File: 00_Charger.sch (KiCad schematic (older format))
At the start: 42 parts, among them J401 TB001-500-02BE CUI_Devices, Q401 NTK3043N, Q402 FDD4685-F085, U401 MAX1873TEEE, U402 PC827

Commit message: fertig zum routen
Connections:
- net GNDPWR is gone; now on net GND: J401.1 (Pin_1)
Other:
- note removed: "GND über Shunt verbinden"
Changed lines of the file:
@@
 Text Notes 3500 1600 0    50   ~ 0
 Spannung 20V in Ladekabel
-$Comp
-L power:GNDPWR #PWR0401
-U 1 1 5E8B9696
-P 2250 2600
-F 0 "#PWR0401" H 2250 2400 50  0001 C CNN
-F 1 "GNDPWR" H 2254 2446 50  0000 C CNN
-F 2 "" H 2250 2550 50  0001 C CNN
-F 3 "" H 2250 2550 50  0001 C CNN
-	1    2250 2600
-	1    0    0    -1
-$EndComp
-Wire Wire Line
-	2250 2600 2250 2300
-Text Notes 1850 1900 0    50   ~ 0
-GND über Shunt verbinden
 Text Label 3300 2200 0    50   ~ 0
 DC_20V_POWER_SUPPLY
@@
 Wire Wire Line
 	9000 3900 9000 3750
+$Comp
+L power:GND #PWR0191
+U 1 1 5E980EB1
+P 2250 3100
+F 0 "#PWR0191" H 2250 2850 50  0001 C CNN
+F 1 "GND" H 2255 2927 50  0000 C CNN
+F 2 "" H 2250 3100 50  0001 C CNN
+F 3 "" H 2250 3100 50  0001 C CNN
+	1    2250 3100
+	1    0    0    -1
+$EndComp
+Wire Wire Line
+	2250 2300 2250 3100
 $EndSCHEMATC

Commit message: Fertig zum letzten Check vor Bestellung
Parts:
- C411: footprint Capacitor_SMD:CP_Elec_5x5.4 -> Capacitor_THT:CP_Radial_D6.3mm_P2.50mm
- C412: footprint Capacitor_SMD:CP_Elec_5x5.4 -> Capacitor_THT:CP_Radial_D5.0mm_P2.50mm
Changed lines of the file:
@@
 F 0 "C411" H 8741 4196 50  0000 L CNN
 F 1 "68u" H 8741 4105 50  0000 L CNN
-F 2 "Capacitor_SMD:CP_Elec_5x5.4" H 8650 4150 50  0001 C CNN
+F 2 "Capacitor_THT:CP_Radial_D6.3mm_P2.50mm" H 8650 4150 50  0001 C CNN
 F 3 "~" H 8650 4150 50  0001 C CNN
 	1    8650 4150
@@
 F 0 "C412" H 9391 3546 50  0000 L CNN
 F 1 "47u" H 9391 3455 50  0000 L CNN
-F 2 "Capacitor_SMD:CP_Elec_5x5.4" H 9300 3500 50  0001 C CNN
+F 2 "Capacitor_THT:CP_Radial_D5.0mm_P2.50mm" H 9300 3500 50  0001 C CNN
 F 3 "~" H 9300 3500 50  0001 C CNN
 	1    9300 3500

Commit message: Board abgeschickt
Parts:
- C401: value 1u -> 1uF
- C402, C403, C405, C406: value 220n -> 220nF
- C404: value 2.2u -> 2.2uF
- C407, C408: value 47n -> 47nF
- C409: value 1n -> 1nF
- C410: value 0.1u -> 100nF
- C411: value 68u -> 68uF
- C412: value 47u -> 68uF
- HS401, HS402, HS403: value Heatsink_Pad -> 573300D00000G
- R417: value 100K -> 1M
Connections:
- net CHARGER_DISABLE: now also R417.1
- net at Q401.1 (G), R415.2: no longer R417.1
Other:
- moved on the sheet: R415, R417
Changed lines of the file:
@@
 P 7350 4450
 F 0 "C408" V 7400 4100 50  0000 C CNN
-F 1 "47n" V 7400 4300 50  0000 C CNN
+F 1 "47nF" V 7400 4300 50  0000 C CNN
 F 2 "Capacitor_SMD:C_0603_1608Metric_Pad1.05x0.95mm_HandSolder" H 7350 4450 50  0001 C CNN
 F 3 "~" H 7350 4450 50  0001 C CNN
@@
 P 5050 4050
 F 0 "C401" H 4958 4004 50  0000 R CNN
-F 1 "1u" H 4958 4095 50  0000 R CNN
+F 1 "1uF" H 4958 4095 50  0000 R CNN
 F 2 "Capacitor_SMD:C_0603_1608Metric_Pad1.05x0.95mm_HandSolder" H 5050 4050 50  0001 C CNN
 F 3 "~" H 5050 4050 50  0001 C CNN
@@
 P 7350 4950
 F 0 "C409" V 7400 4650 50  0000 C CNN
-F 1 "1n" V 7400 4850 50  0000 C CNN
+F 1 "1nF" V 7400 4850 50  0000 C CNN
 F 2 "Capacitor_SMD:C_0603_1608Metric_Pad1.05x0.95mm_HandSolder" H 7350 4950 50  0001 C CNN
 F 3 "~" H 7350 4950 50  0001 C CNN
@@
 P 5450 3100
 F 0 "C402" V 5221 3100 50  0000 C CNN
-F 1 "220n" V 5312 3100 50  0000 C CNN
+F 1 "220nF" V 5312 3100 50  0000 C CNN
 F 2 "Capacitor_SMD:C_0603_1608Metric_Pad1.05x0.95mm_HandSolder" H 5450 3100 50  0001 C CNN
 F 3 "~" H 5450 3100 50  0001 C CNN
@@
 P 7350 4300
 F 0 "C407" V 7400 3950 50  0000 C CNN
-F 1 "47n" V 7400 4150 50  0000 C CNN
+F 1 "47nF" V 7400 4150 50  0000 C CNN
 F 2 "Capacitor_SMD:C_0603_1608Metric_Pad1.05x0.95mm_HandSolder" H 7350 4300 50  0001 C CNN
 F 3 "~" H 7350 4300 50  0001 C CNN
@@
 U 1 1 5E7803AB
 P 7850 4600
-F 0 "C410" V 7950 4350 50  0000 C CNN
-F 1 "0.1u" V 7900 4500 50  0000 C CNN
+F 0 "C410" V 7750 4450 50  0000 C CNN
+F 1 "100nF" V 7650 4450 50  0000 C CNN
 F 2 "Capacitor_SMD:C_0603_1608Metric_Pad1.05x0.95mm_HandSolder" H 7850 4600 50  0001 C CNN
 F 3 "~" H 7850 4600 50  0001 C CNN
@@
 P 5700 2900
 F 0 "C403" V 5471 2900 50  0000 C CNN
-F 1 "220n" V 5562 2900 50  0000 C CNN
+F 1 "220nF" V 5562 2900 50  0000 C CNN
 F 2 "Capacitor_SMD:C_0603_1608Metric_Pad1.05x0.95mm_HandSolder" H 5700 2900 50  0001 C CNN
 F 3 "~" H 5700 2900 50  0001 C CNN
@@
 P 6600 2450
 F 0 "C404" V 6371 2450 50  0000 C CNN
-F 1 "2.2u" V 6462 2450 50  0000 C CNN
+F 1 "2.2uF" V 6462 2450 50  0000 C CNN
 F 2 "Capacitor_SMD:C_0603_1608Metric_Pad1.05x0.95mm_HandSolder" H 6600 2450 50  0001 C CNN
 F 3 "~" H 6600 2450 50  0001 C CNN
@@
 P 7300 3000
 F 0 "C405" H 7208 2954 50  0000 R CNN
-F 1 "220n" H 7208 3045 50  0000 R CNN
+F 1 "220nF" H 7208 3045 50  0000 R CNN
 F 2 "Capacitor_SMD:C_0603_1608Metric_Pad1.05x0.95mm_HandSolder" H 7300 3000 50  0001 C CNN
 F 3 "~" H 7300 3000 50  0001 C CNN
@@
 P 7300 3450
 F 0 "C406" H 7208 3404 50  0000 R CNN
-F 1 "220n" H 7208 3495 50  0000 R CNN
+F 1 "220nF" H 7208 3495 50  0000 R CNN
 F 2 "Capacitor_SMD:C_0603_1608Metric_Pad1.05x0.95mm_HandSolder" H 7300 3450 50  0001 C CNN
 F 3 "~" H 7300 3450 50  0001 C CNN
@@
 P 8650 4150
 F 0 "C411" H 8741 4196 50  0000 L CNN
-F 1 "68u" H 8741 4105 50  0000 L CNN
+F 1 "68uF" H 8741 4105 50  0000 L CNN
 F 2 "Capacitor_THT:CP_Radial_D6.3mm_P2.50mm" H 8650 4150 50  0001 C CNN
 F 3 "~" H 8650 4150 50  0001 C CNN
@@
 Text GLabel 3600 3950 0    50   Input ~ 0
 CHARGER_DISABLE
-Wire Wire Line
-	3950 3950 4100 3950
 Text Notes 8900 2450 0    50   ~ 0
 R_CSB - Charge Current Limit\n68m: Icharge = 0.2V/R_CSB = 3A\nfür 2 Zellen Parallel = 0.5Charging Rate\n
@@
 P 9300 3500
 F 0 "C412" H 9391 3546 50  0000 L CNN
-F 1 "47u" H 9391 3455 50  0000 L CNN
+F 1 "68uF" H 9391 3455 50  0000 L CNN
 F 2 "Capacitor_THT:CP_Radial_D5.0mm_P2.50mm" H 9300 3500 50  0001 C CNN
 F 3 "~" H 9300 3500 50  0001 C CNN
@@
 L Device:R_Small R415
 U 1 1 5ECEF6C1
-P 3850 3950
-F 0 "R415" V 3750 4000 50  0000 R CNN
-F 1 "10k" V 3650 4000 50  0000 R CNN
-F 2 "Resistor_SMD:R_0603_1608Metric_Pad1.05x0.95mm_HandSolder" H 3850 3950 50  0001 C CNN
-F 3 "~" H 3850 3950 50  0001 C CNN
-	1    3850 3950
+P 4000 3950
+F 0 "R415" V 3900 4000 50  0000 R CNN
+F 1 "10k" V 3800 4000 50  0000 R CNN
+F 2 "Resistor_SMD:R_0603_1608Metric_Pad1.05x0.95mm_HandSolder" H 4000 3950 50  0001 C CNN
+F 3 "~" H 4000 3950 50  0001 C CNN
+	1    4000 3950
 	0    -1   -1   0
 $EndComp
 Wire Wire Line
-	3750 3950 3600 3950
+	3900 3950 3800 3950
 $Comp
 L Device:R_Small R417
 U 1 1 5EE5F4E2
-P 4100 4350
-F 0 "R417" H 4159 4396 50  0000 L CNN
-F 1 "100K" H 4159 4305 50  0000 L CNN
-F 2 "Resistor_SMD:R_0603_1608Metric_Pad1.05x0.95mm_HandSolder" H 4100 4350 50  0001 C CNN
-F 3 "~" H 4100 4350 50  0001 C CNN
-	1    4100 4350
-	1    0    0    -1
-$EndComp
-Wire Wire Line
-	4100 4250 4100 3950
-Connection ~ 4100 3950
-Wire Wire Line
-	4100 3950 4200 3950
+P 3800 4350
+F 0 "R417" H 3859 4396 50  0000 L CNN
+F 1 "1M" H 3859 4305 50  0000 L CNN
+F 2 "Resistor_SMD:R_0603_1608Metric_Pad1.05x0.95mm_HandSolder" H 3800 4350 50  0001 C CNN
+F 3 "~" H 3800 4350 50  0001 C CNN
+	1    3800 4350
+	1    0    0    -1
+$EndComp
 $Comp
 L power:GND #PWR0407
 U 1 1 5EE6150A
-P 4100 5200
-F 0 "#PWR0407" H 4100 4950 50  0001 C CNN
-F 1 "GND" H 4105 5027 50  0000 C CNN
-F 2 "" H 4100 5200 50  0001 C CNN
-F 3 "" H 4100 5200 50  0001 C CNN
-	1    4100 5200
-	1    0    0    -1
-$EndComp
-Wire Wire Line
-	4100 5200 4100 4450
+P 3800 5200
+F 0 "#PWR0407" H 3800 4950 50  0001 C CNN
+F 1 "GND" H 3805 5027 50  0000 C CNN
+F 2 "" H 3800 5200 50  0001 C CNN
+F 3 "" H 3800 5200 50  0001 C CNN
+	1    3800 5200
+	1    0    0    -1
+$EndComp
+Wire Wire Line
+	3800 5200 3800 4450
 Connection ~ 5550 2200
 $Comp
@@
 P 4750 1450
 F 0 "HS401" H 4891 1491 50  0000 L CNN
-F 1 "Heatsink_Pad" H 4891 1400 50  0000 L CNN
+F 1 "573300D00000G" H 4891 1400 50  0000 L CNN
 F 2 "Heatsink:Heatsink_AAVID_573300D00010G_TO-263" H 4762 1400 50  0001 C CNN
 F 3 "~" H 4762 1400 50  0001 C CNN
@@
 P 8450 3400
 F 0 "HS403" H 8500 4000 50  0000 L CNN
-F 1 "Heatsink_Pad" H 8500 3900 50  0000 L CNN
+F 1 "573300D00000G" H 8500 3900 50  0000 L CNN
 F 2 "Heatsink:Heatsink_AAVID_573300D00010G_TO-263" H 8462 3350 50  0001 C CNN
 F 3 "~" H 8462 3350 50  0001 C CNN
@@
 P 8150 3400
 F 0 "HS402" H 8150 4000 50  0000 L CNN
-F 1 "Heatsink_Pad" H 7950 3900 50  0000 L CNN
+F 1 "573300D00000G" H 7950 3900 50  0000 L CNN
 F 2 "Heatsink:Heatsink_AAVID_573300D00010G_TO-263" H 8162 3350 50  0001 C CNN
 F 3 "~" H 8162 3350 50  0001 C CNN
@@
 Wire Wire Line
 	2250 2300 2250 3100
+Wire Wire Line
+	4100 3950 4200 3950
+Wire Wire Line
+	3800 4250 3800 3950
+Connection ~ 3800 3950
+Wire Wire Line
+	3800 3950 3600 3950
 $EndSCHEMATC

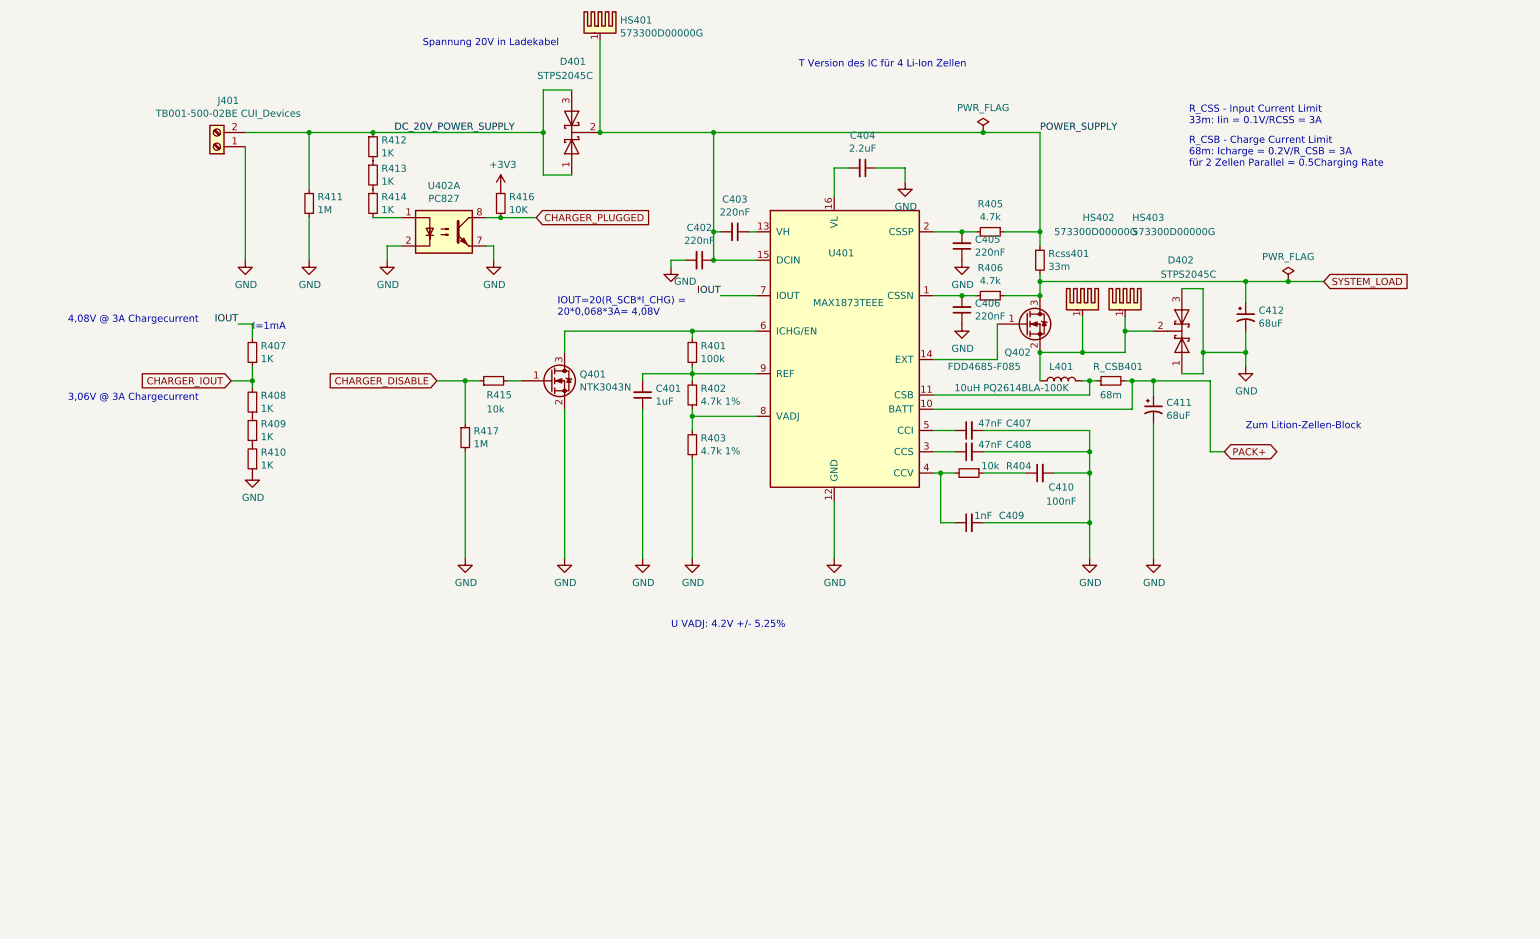
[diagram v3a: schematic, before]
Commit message: mute and stdby tda7498 geändert, tda7418 durch tda7719 ersetzt, xs3868 durch bk8000l ersetzt, 3v3 stepdown statt LDO. BMS gelöscht.  TODO: Möglichkeit stepup und stepdown als modul aufzusetzen
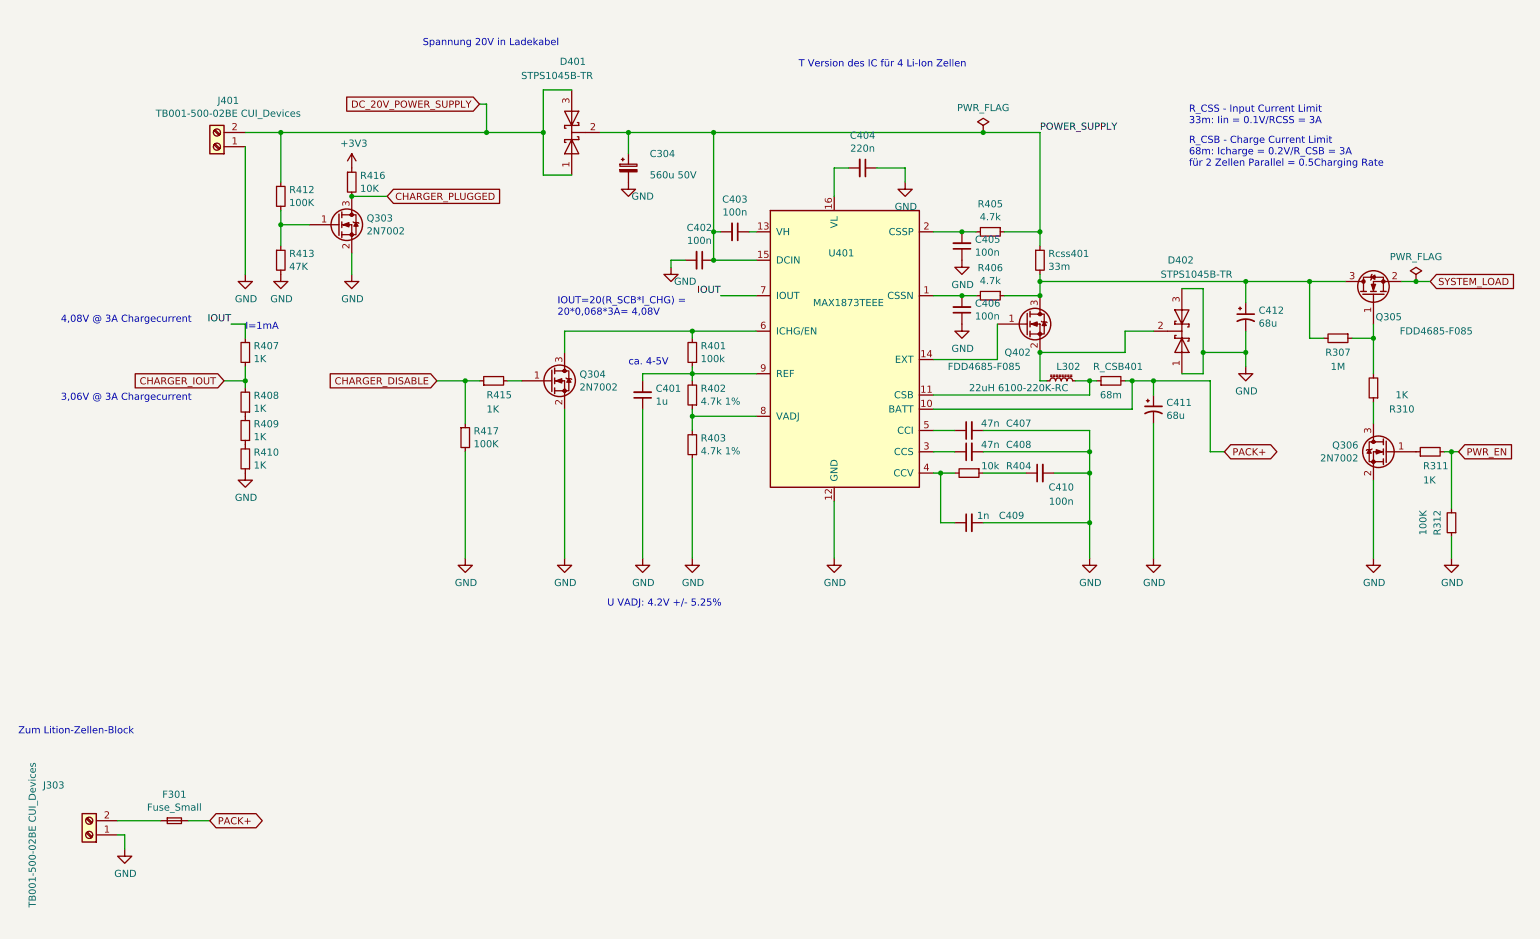
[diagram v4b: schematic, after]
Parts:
- removed HS401, HS402, HS403: 573300D00000G, Heatsink:Heatsink_AAVID_573300D00010G_TO-263, symbol Mechanical:Heatsink_Pad
- removed L401: 10uH PQ2614BLA-100K, Inductor_SMD:PQ2617BHA-330K, symbol Device:L
- removed Q401: NTK3043N, Package_TO_SOT_SMD:SOT-723, symbol Device:Q_NMOS_GSD
- removed R411: 1M, Resistor_SMD:R_0603_1608Metric_Pad1.05x0.95mm_HandSolder, symbol Device:R_Small
- removed R414: 1K, Resistor_SMD:R_0603_1608Metric_Pad1.05x0.95mm_HandSolder, symbol Device:R_Small
- removed U402: PC827, Package_DIP:DIP-8_W7.62mm_SMDSocket_SmallPads, symbol Isolator:PC827
- added C304: 560u 50V, Capacitor_THT:CP_Radial_D12.5mm_P5.00mm, symbol Device:CP_Small
- added F301: Fuse_Small, Fuse:Fuseholder_Cylinder-5x20mm_Schurter_0031-8002_Horizontal_Open, symbol Device:Fuse_Small
- added J303: TB001-500-02BE CUI_Devices, TerminalBlock_RND:TerminalBlock_RND_205-00045_1x02_P5.00mm_Horizontal, symbol Connector:Screw_Terminal_01x02
- added L302: 22uH 6100-220K-RC, Inductor_THT:L_Radial_D12.0mm_P6.00mm_MuRATA_1900R, symbol Device:L_Core_Ferrite_Small
- added Q303, Q304, Q306: 2N7002, Package_TO_SOT_SMD:SOT-23, symbol Transistor_FET:2N7002
- added Q305: FDD4685-F085, Package_TO_SOT_SMD:TO-252-2, symbol Device:Q_NMOS_GSD
- added R307: 1M, Resistor_SMD:R_0603_1608Metric_Pad1.05x0.95mm_HandSolder, symbol Device:R_Small
- added R310, R311: 1K, Resistor_SMD:R_0603_1608Metric_Pad1.05x0.95mm_HandSolder, symbol Device:R_Small
- added R312: 100K, Resistor_SMD:R_0603_1608Metric_Pad1.05x0.95mm_HandSolder, symbol Device:R_Small
- C401: value 1uF -> 1u
- C402, C403, C405, C406: value 220nF -> 100n
- C404: value 2.2uF -> 220n
- C407, C408: value 47nF -> 47n
- C409: value 1nF -> 1n
- C410: value 100nF -> 100n
- C411, C412: value 68uF -> 68u
- D401, D402: value STPS2045C -> STPS1045B-TR; footprint Package_TO_SOT_SMD:TO-263-2 -> Package_TO_SOT_SMD:TO-252-2
- Q402: footprint Package_TO_SOT_SMD:TO-263-2 -> Package_TO_SOT_SMD:TO-252-2
- R412: value 1K -> 100K
- R413: value 1K -> 47K
- R415: value 10k -> 1K
- R417: value 1M -> 100K
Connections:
- net CHARGER_PLUGGED: now also Q303.3 (D)
- net GND: now also R413.2, C304.2, J303.1 (Pin_1), Q303.2 (S), Q304.2 (S), Q306.2 (S), R312.1
- net PACK+: now also F301.2
- net POWER_SUPPLY: now also C304.1
- net SYSTEM_LOAD: now also Q305.2 (S); no longer C412.1, Q402.3 (D), R406.1, Rcss401.2
- net at R_CSB401.1, U401.11 (CSB): now also L302.2
- net at R401.2, U401.6 (ICHG/EN): now also Q304.3 (D)
- net at D402.2 (K), Q402.2 (S): now also L302.1
- net at R415.2: now also Q304.1 (G)
- net at R412.2, R413.1: now also Q303.1 (G)
- new net: C412.1, Q305.3 (D), Q402.3 (D), R307.2, R406.1, Rcss401.2
- new net: F301.1, J303.2 (Pin_2)
- new net: Q305.1 (G), R307.1, R310.2
- new net: Q306.3 (D), R310.1
- new net: Q306.1 (G), R311.1
- new net PWR_EN: R311.2, R312.2
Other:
- note added: "ca. 4-5V"
- moved on the sheet: R407, R408, R409, R410, R412, R413, R416
